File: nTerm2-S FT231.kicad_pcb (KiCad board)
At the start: 2 copper layers, 147.3 x 55.9 mm, 126 parts, among them J1 VGA, J2 Keyboard, J3 Mouse, J4 Line-out/Speaker, J5 RS-232 V.24, J6 USB_C_Receptacle_USB2.0_16P, J7 Line-out/Speaker, K1 IM41 3V, K2 IM41 3V, K3 IM41 3V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

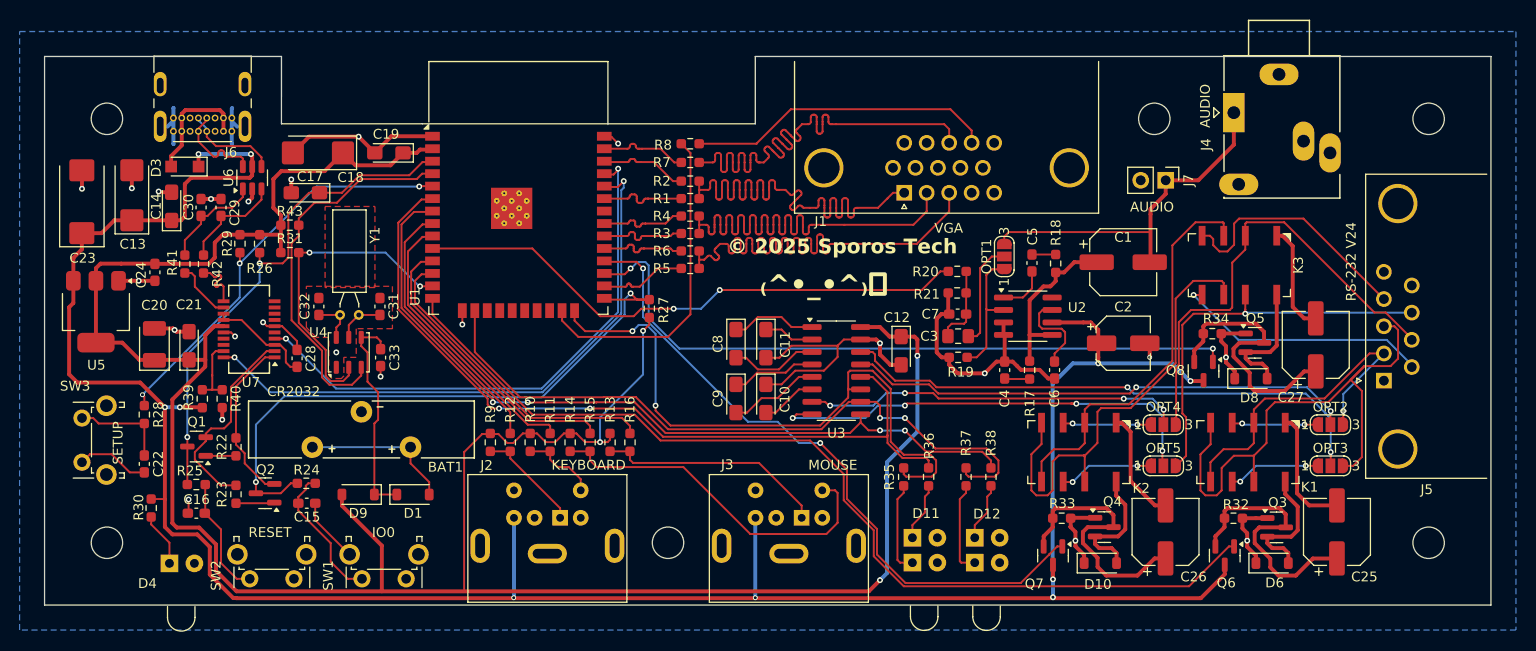
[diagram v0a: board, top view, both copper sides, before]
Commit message: nTerm2-S V0.11
* Added a footprint for a volume control potmeter.
* Improved routing around R29, R26, R43 and R31. It's not super still, but better than routing 2 traces under a resistor.
* New documentation, including a proper render that will help with placing components.
* Added bunch of 3D packages
* Resolved some library issues
* Created fabrication files for v0.11
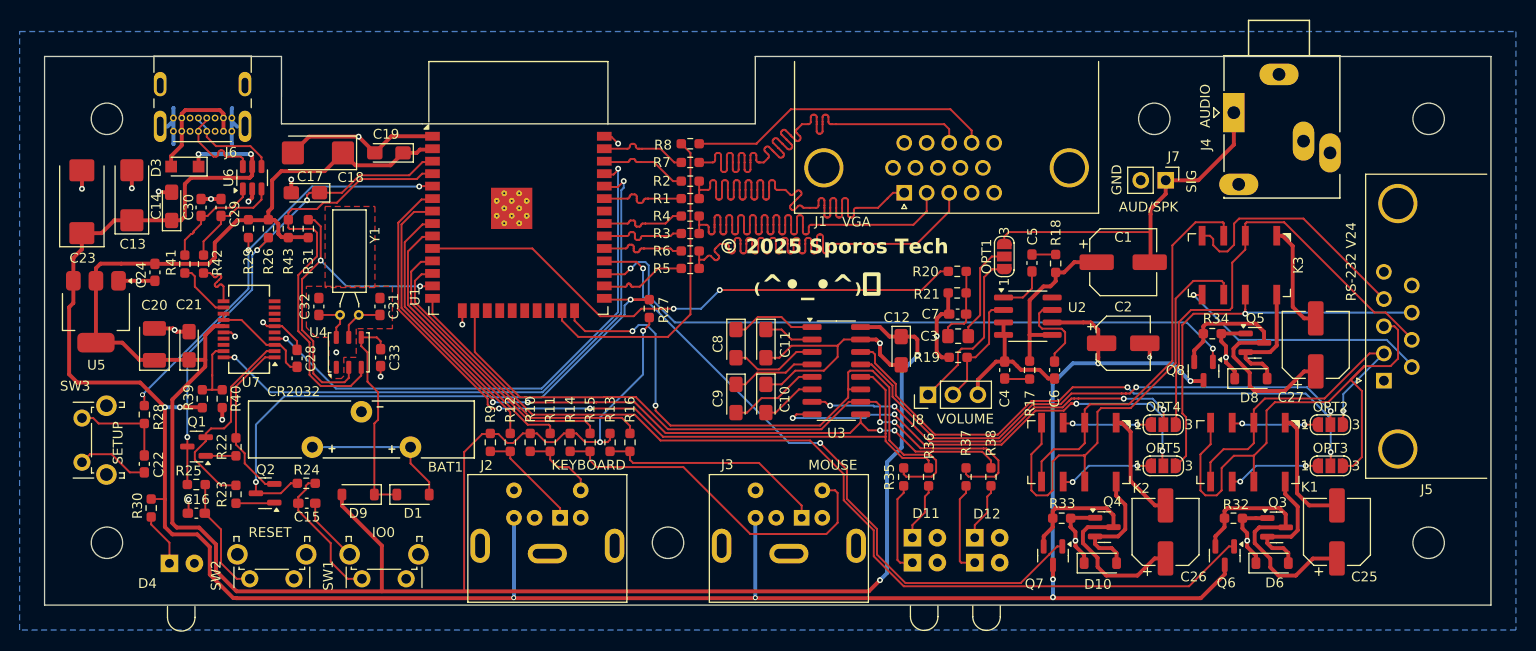
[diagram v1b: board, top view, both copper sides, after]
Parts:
- added J8: 10K pot, Connector_PinHeader_2.54mm:PinHeader_1x03_P2.54mm_Vertical, F.Cu at (164.1, 106.4)
- moved R31 3.08 mm to (101.0, 89.5), turned to 90 degrees
- moved R26 1.77 mm to (96.9, 89.5)
- moved R29 1.76 mm to (94.9, 89.5)
- moved R43 0.39 mm to (98.9, 89.5), turned to 90 degrees
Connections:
- OPT1 pad 1: Net-(OPT1-A) -> Net-(J8-Pin_1)
- R19 pad 2: Net-(OPT1-A) -> Net-(J8-Pin_2)
- U2 pad 2: Net-(OPT1-A) -> Net-(J8-Pin_2)
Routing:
- net Net-(J8-Pin_1): track 0.00 -> 17.3 mm
- net Net-(OPT1-A): track 13.5 -> 0.00 mm
- net Net-(J8-Pin_2): track 0.00 -> 12.0 mm
- net ~{INT}: track 38.8 -> 43.7 mm
- net /TxD: track 55.9 -> 60.7 mm
- net /RxD: track 51.8 -> 56.2 mm
- net ONE-WIRE: track 32.4 -> 35.5 mm
- net /CTS: track 46.4 -> 49.0 mm
- net /RTS: track 39.0 -> 41.6 mm
- net GND: track 146.9 -> 144.6 mm
- net +3V3: track 259.0 -> 260.3 mm
- net RTS_CTS_OR_DTR_DSR: track 70.6 -> 69.3 mm
- net REVERSE_RTS_CTS_DTR_DSR: track 67.9 -> 66.7 mm
- net IO0: track 62.9 -> 62.0 mm
- net EN: track 50.2 -> 49.5 mm, vias 2 -> 3
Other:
- board text added: "AUD/SPK"
- board text added: "GND"
- board text added: "SIG"
- board text added: "VOLUME"

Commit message: Big booboo! I forgot about the 5K1 resistors necessary on the CC lines of the USB-C connector. With those, the USB-C will not give power to the board. If you use a USB-A to USB-C cable, it works great. And that's what I've been doing for months. So I never noticed that it didn't work with USB-C to USB-C. I remember making a mental note about it at some time, but I never did add them. So we need a V0.12 to fix that. - Added the 5K1 resistors for the CC lines of the USB-C connector. - Refactored the placement and routing around the USBLC6-2SC6 to make room for the two 5K1 resistors. - Refactored the 3V3 power distribution to the FT231 and the ESP32. - Changed the position of the silkscreen texts. Added the URLs to all the repositories. Made a big logo on the back of the PCB now. - Revision 0.12 - Generated gerbers and drill files. - Updated the images.
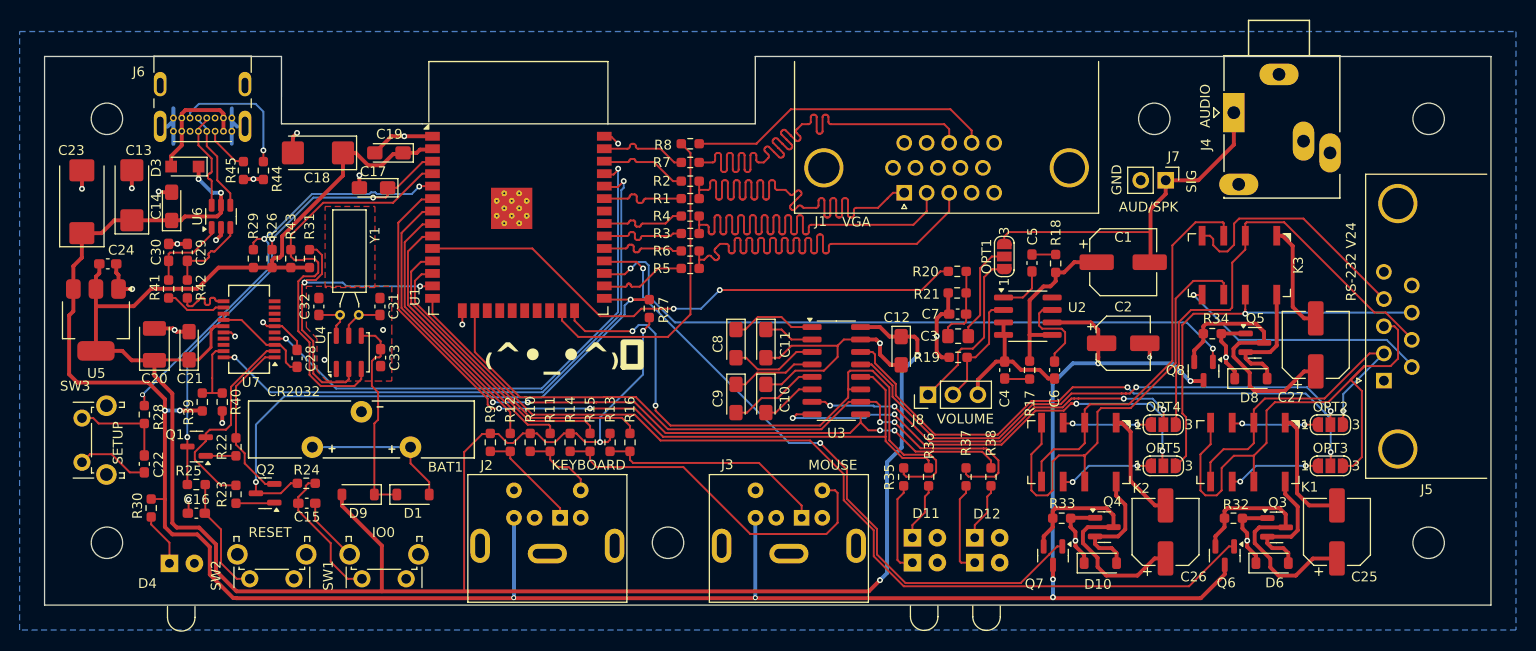
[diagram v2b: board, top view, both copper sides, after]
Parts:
- added R44: 5.1k, nTerm2-S:R_0603_1608Metric_Pad0.98x0.95mm_HandSolder, F.Cu at (96.4, 83.6)
- added R45: 5.1k, nTerm2-S:R_0603_1608Metric_Pad0.98x0.95mm_HandSolder, F.Cu at (94.4, 83.6)
- U4: footprint nTerm2-S:TSOC-6_3.76x3.94mm_P1.27mm -> nTerm2-S:TSOC-6_3.76x3.94mm_P1.27mm_handsolder
- moved C17 6.96 mm to (107.6, 85.3)
- moved C29 5.71 mm to (88.6, 91.9)
- moved C30 5.64 mm to (86.7, 91.9)
- moved U6 5.06 mm to (92.1, 88.3)
- moved C24 4.88 mm to (80.5, 93.1), turned to 0 degrees
- moved R29 3.09 mm to (95.4, 92.6), turned to 90 degrees
- moved R26 3.07 mm to (97.3, 92.6), turned to 90 degrees
- moved R43 3.06 mm to (99.2, 92.6)
- moved R31 3.05 mm to (101.1, 92.6)
- moved R41 3.03 mm to (86.7, 95.7)
- moved R42 3.03 mm to (88.6, 95.7)
- moved U5 0.84 mm to (79.3, 98.8)
- moved R39 0.33 mm to (90.2, 107.2)
- moved R40 0.33 mm to (92.2, 107.2)
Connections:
- J6 pad A5: unconnected-(J6-CC1-PadA5) -> Net-(J6-CC1)
- J6 pad B5: unconnected-(J6-CC2-PadB5) -> Net-(J6-CC2)
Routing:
- net Net-(J6-CC2): track 0.00 -> 13.7 mm, vias 0 -> 1
- net +5V: track 251.3 -> 242.4 mm
- net GND: track 144.6 -> 137.6 mm, vias 23 -> 25
- net Net-(J6-CC1): track 0.00 -> 4.84 mm
- net Net-(C29-Pad1): track 10.6 -> 8.53 mm
- net Net-(C30-Pad1): track 10.6 -> 8.55 mm
- net ONE-WIRE: track 35.5 -> 33.8 mm
- net +3V3: track 260.3 -> 259.0 mm
- net Net-(D1-K): track 22.1 -> 21.1 mm
- net ~{INT}: track 43.7 -> 42.8 mm
- net Net-(U1-IO39/SENSVN): track 43.2 -> 44.0 mm
- net EN: track 49.5 -> 48.7 mm
- net Net-(J6-D--PadA7): track 9.62 -> 10.2 mm
- net Net-(J6-D+-PadA6): track 9.66 -> 10.2 mm
- net CTS_2: track 81.3 -> 80.8 mm
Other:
- board text added: "https://github.com/RetepV/nTerm2-S-FT231 https://github.com/RetepV/SporosTerm"
- board text added: "© 2025, 2026 Sporos Tech, Peter de Vroomen"
- board text removed: "© 2025 Sporos Tech"
